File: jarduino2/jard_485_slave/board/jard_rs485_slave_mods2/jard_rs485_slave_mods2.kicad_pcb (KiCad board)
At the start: 2 copper layers, 79.2 x 30 mm, 46 parts, among them J1 POWER, J3 Débit, J4 Niveaux, J6 EV1, Q4 BPC_FMMT38C, Q6 P03P4L-04, U1 MAX485E, U6 BPC_DHT22

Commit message: Finitions avant production
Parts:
- added TP6: TestPoint, TestPoint:TestPoint_Pad_D1.5mm, B.Cu at (124.0, 103.9)
- added TP7: TestPoint, TestPoint:TestPoint_Pad_D1.5mm, B.Cu at (123.9, 98.8)
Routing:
- net BUS_A: track 19.9 -> 23.2 mm
- net BUS_B: track 22.2 -> 25.5 mm
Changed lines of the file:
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@@
     )
+  )
+  (footprint "TestPoint:TestPoint_Pad_D1.5mm" (layer "B.Cu")
+    (at 123.96 103.89 180)
+    (descr "SMD pad as test Point, diameter 1.5mm")
+    (tags "test point SMD pad")
+    (property "Price" "0")
+    (property "RefFabricant" "")
+    (property "RefFournisseur" "")
+    (property "Sheetfile" "ES.kicad_sch")
+    (property "Sheetname" "ES")
+    (property "ki_description" "test point")
+    (property "ki_keywords" "test point tp")
+    (attr exclude_from_pos_files)
+    (fp_text reference "TP6" (at 0 1.648) (layer "B.SilkS") hide
+        (effects (font (size 1 1) (thickness 0.15)) (justify mirror))
+    )
+    (fp_text value "TestPoint" (at 0 -1.75) (layer "B.Fab")
+        (effects (font (size 1 1) (thickness 0.15)) (justify mirror))
+    )
+    (fp_text user "${REFERENCE}" (at 0 1.65) (layer "B.Fab")
+        (effects (font (size 1 1) (thickness 0.15)) (justify mirror))
+    )
+    (fp_circle (center 0 0) (end 0 -0.95)
+      (stroke (width 0.12) (type solid)) (fill none) (layer "B.SilkS"))
+    (fp_circle (center 0 0) (end 1.25 0)
+      (stroke (width 0.05) (type solid)) (fill none) (layer "B.CrtYd"))
+    (pad "1" smd circle (at 0 0 180) (size 1.5 1.5) (layers "B.Cu" "B.Mask")
+      (net 17 "BUS_B") (pinfunction "1") (pintype "passive"))
   )
   (footprint "LED_THT:LED_D3.0mm_FlatTop" (layer "B.Cu")
@@
   )
   (footprint "TestPoint:TestPoint_Pad_D1.5mm" (layer "B.Cu")
+    (at 123.93 98.82 180)
+    (descr "SMD pad as test Point, diameter 1.5mm")
+    (tags "test point SMD pad")
+    (property "Price" "0")
+    (property "RefFabricant" "")
+    (property "RefFournisseur" "")
+    (property "Sheetfile" "ES.kicad_sch")
+    (property "Sheetname" "ES")
+    (property "ki_description" "test point")
+    (property "ki_keywords" "test point tp")
+    (attr exclude_from_pos_files)
+    (fp_text reference "TP7" (at 0 1.648) (layer "B.SilkS") hide
+        (effects (font (size 1 1) (thickness 0.15)) (justify mirror))
+    )
+    (fp_text value "TestPoint" (at 0 -1.75) (layer "B.Fab")
+        (effects (font (size 1 1) (thickness 0.15)) (justify mirror))
+    )
+    (fp_text user "${REFERENCE}" (at 0 1.65) (layer "B.Fab")
+        (effects (font (size 1 1) (thickness 0.15)) (justify mirror))
+    )
+    (fp_circle (center 0 0) (end 0 -0.95)
+      (stroke (width 0.12) (type solid)) (fill none) (layer "B.SilkS"))
+    (fp_circle (center 0 0) (end 1.25 0)
+      (stroke (width 0.05) (type solid)) (fill none) (layer "B.CrtYd"))
+    (pad "1" smd circle (at 0 0 180) (size 1.5 1.5) (layers "B.Cu" "B.Mask")
+      (net 16 "BUS_A") (pinfunction "1") (pintype "passive"))
+  )
+  (footprint "TestPoint:TestPoint_Pad_D1.5mm" (layer "B.Cu")
     (at 154.97 115.24 90)
     (descr "SMD pad as test Point, diameter 1.5mm")
@@
   (gr_rect (start 113.39 86.8) (end 192.39 116.8)
     (stroke (width 0.1) (type solid)) (fill none) (layer "User.1"))
+  (gr_text "A" (at 123.38 97.4 270) (layer "B.SilkS")
+    (effects (font (size 0.8 0.8) (thickness 0.1)) (justify left bottom mirror))
+  )
   (gr_text "TX" (at 145.288 92.202 90) (layer "B.SilkS")
     (effects (font (size 0.8 0.8) (thickness 0.1)) (justify left bottom mirror))
@@
     (effects (font (size 0.8 0.8) (thickness 0.1)) (justify left bottom mirror))
   )
+  (gr_text "Esclave OYA\nRev G0\nBPC 2024" (at 116.41 105.8 -90) (layer "B.SilkS")
+    (effects (font (size 1 1) (thickness 0.15)) (justify left bottom mirror))
+  )
   (gr_text "TEN" (at 145.25 97.18 90) (layer "B.SilkS")
     (effects (font (size 0.8 0.8) (thickness 0.1)) (justify left bottom mirror))
   )
+  (gr_text "B" (at 123.46 106.14 270) (layer "B.SilkS")
+    (effects (font (size 0.8 0.8) (thickness 0.1)) (justify left bottom mirror))
+  )
   (gr_text "+12V" (at 117.96 95.68 -90) (layer "B.SilkS")
     (effects (font (size 0.8 0.8) (thickness 0.1)) (justify left bottom mirror))
@@
     (effects (font (size 1 1) (thickness 0.15)) (justify left bottom))
   )
-  (gr_text "05/05/2024" (at 114.32 107.73 270) (layer "F.SilkS")
+  (gr_text "05/05/2024" (at 114.55 107.41 270) (layer "F.SilkS")
     (effects (font (size 0.8 0.8) (thickness 0.1)) (justify left bottom))
   )
@@
     (effects (font (size 0.8 0.8) (thickness 0.15)) (justify left bottom))
   )
-  (gr_text "Esclave OYA\nRev G0\nBPC 2024" (at 114.12 89.4 270) (layer "F.SilkS")
+  (gr_text "Esclave OYA\nRev G0\nBPC 2024" (at 114.77 89.8 270) (layer "F.SilkS")
     (effects (font (size 1 1) (thickness 0.15)) (justify left bottom))
   )
@@
   (via (at 141.83 104.4) (size 0.8) (drill 0.4) (layers "F.Cu" "B.Cu") (free) (net 2))
   (via (at 188.74 106.29) (size 0.8) (drill 0.4) (layers "F.Cu" "B.Cu") (net 2))
-  (via (at 114.9 98.04) (size 0.8) (drill 0.4) (layers "F.Cu" "B.Cu") (free) (net 2))
+  (via (at 114.87 98.48) (size 0.8) (drill 0.4) (layers "F.Cu" "B.Cu") (free) (net 2))
   (via (at 180.18 96.16) (size 0.8) (drill 0.4) (layers "F.Cu" "B.Cu") (free) (net 2))
   (via (at 128.93 101.47) (size 0.8) (drill 0.4) (layers "F.Cu" "B.Cu") (net 2))
@@
   (segment (start 132.57 99.46) (end 132.57 100.52) (width 0.25) (layer "B.Cu") (net 16))
   (segment (start 134.53 100.52) (end 134.67 100.38) (width 0.25) (layer "B.Cu") (net 16))
+  (segment (start 123.93 98.82) (end 127.27 98.82) (width 0.25) (layer "B.Cu") (net 16))
   (segment (start 131.93 98.82) (end 132.57 99.46) (width 0.25) (layer "B.Cu") (net 16))
   (segment (start 127.27 98.82) (end 131.93 98.82) (width 0.25) (layer "B.Cu") (net 16))
@@
   (segment (start 133.66 101.86) (end 131.62 103.9) (width 0.25) (layer "F.Cu") (net 17))
   (segment (start 127.27 103.9) (end 131.88 103.9) (width 0.25) (layer "B.Cu") (net 17))
+  (segment (start 123.97 103.9) (end 123.96 103.89) (width 0.25) (layer "B.Cu") (net 17))
   (segment (start 134.61 102.42) (end 134.67 102.48) (width 0.25) (layer "B.Cu") (net 17))
   (segment (start 132.58 103.2) (end 132.57 103.19) (width 0.25) (layer "B.Cu") (net 17))
   (segment (start 132.57 103.19) (end 132.57 102.42) (width 0.25) (layer "B.Cu") (net 17))
   (segment (start 132.57 102.42) (end 134.61 102.42) (width 0.25) (layer "B.Cu") (net 17))
+  (segment (start 127.27 103.9) (end 123.97 103.9) (width 0.25) (layer "B.Cu") (net 17))
   (segment (start 131.88 103.9) (end 132.58 103.2) (width 0.25) (layer "B.Cu") (net 17))
   (segment (start 170.54 107.532) (end 170.45 107.442) (width 0.25) (layer "B.Cu") (net 18))

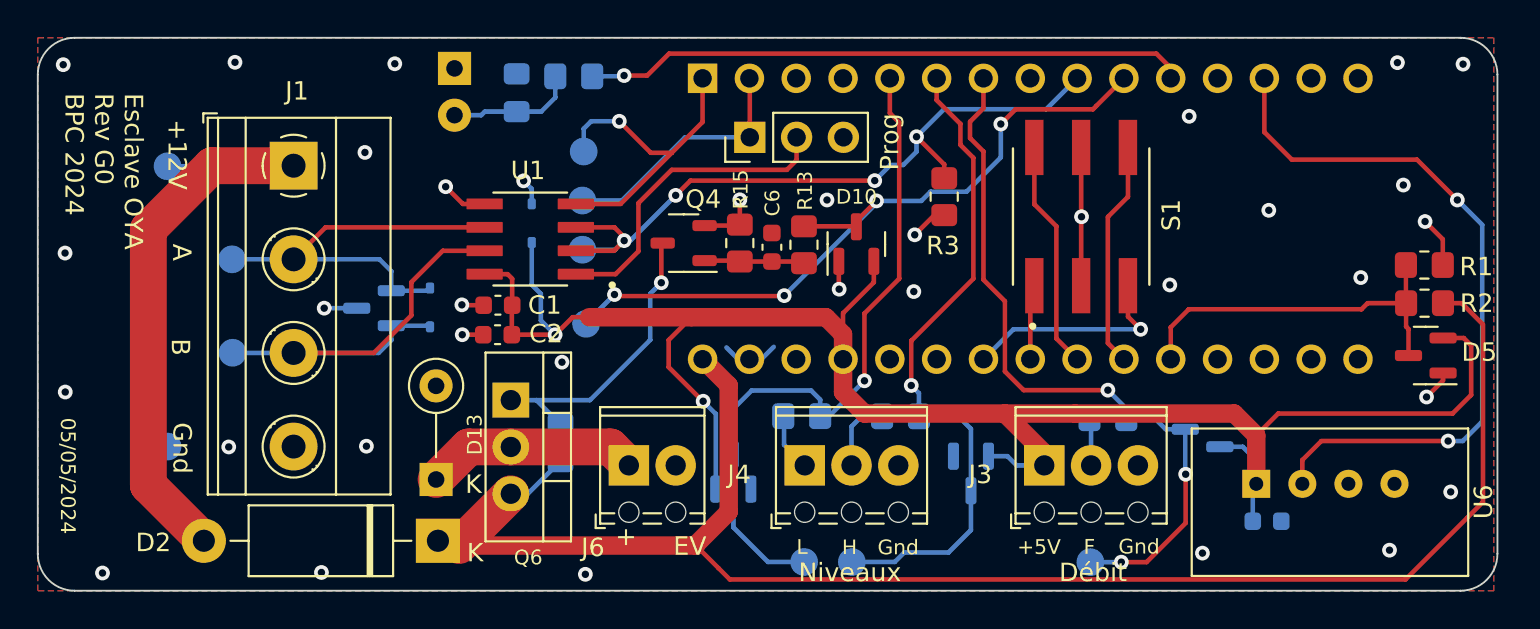
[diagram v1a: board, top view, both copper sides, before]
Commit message: Amélioration découplage RS485, MOS sur autre face
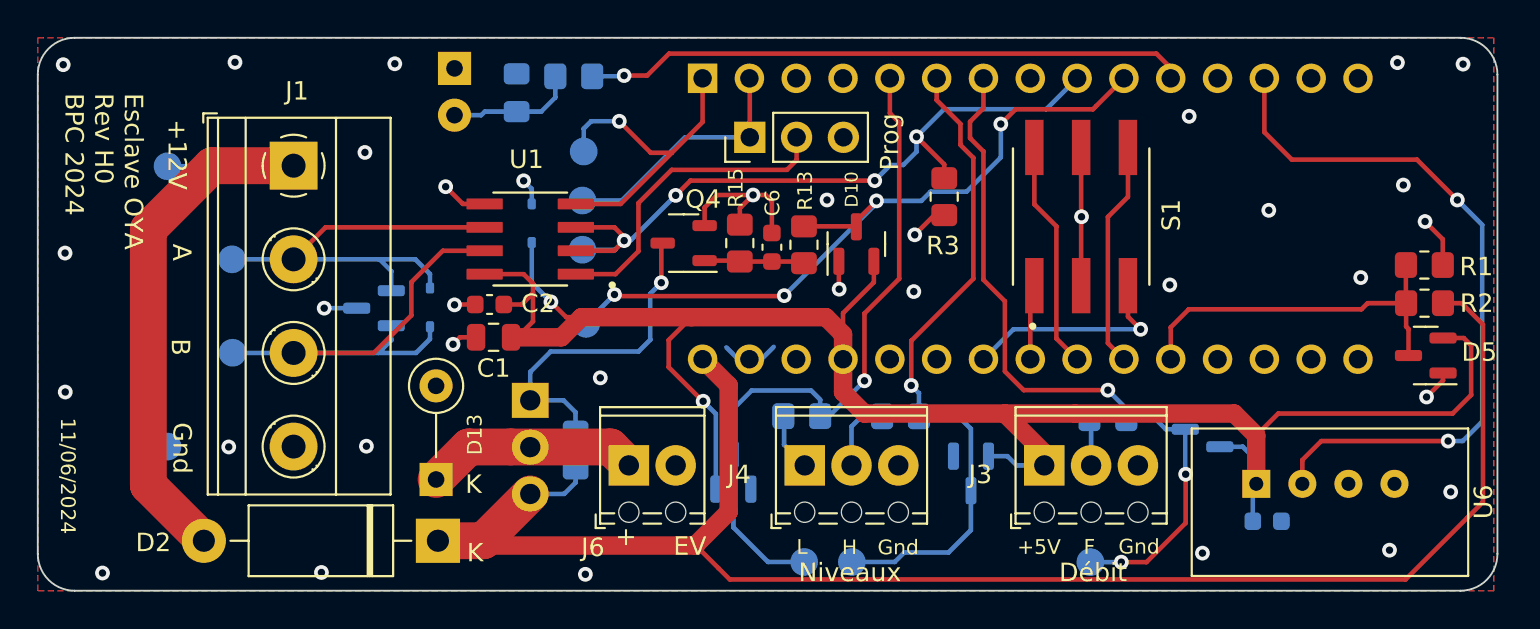
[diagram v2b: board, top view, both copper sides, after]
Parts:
- C1: value 100nF -> 10µF; footprint Capacitor_SMD:C_0603_1608Metric -> Capacitor_SMD:C_0805_2012Metric
- C2, C7: value 1nF -> 100nF
- Q6: moved to B.Cu
- moved C1 1.76 mm to (138.1, 103.0), turned to 180 degrees
- moved C2 1.70 mm to (137.9, 101.3)
- moved Q6 1.06 mm to (140.1, 106.5)
- moved R17 0.91 mm to (142.6, 109.2)
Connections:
- C1 pad 1: GND -> +5V
- C1 pad 2: +5V -> GND
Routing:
- net GND: track 29.9 -> 35.6 mm
- net +5V: track 103.2 -> 107.0 mm
- net POWER_12V: track 89.2 -> 91.3 mm
- net Net-(Q4-C): track 16.3 -> 18.1 mm
- net BUS_A: track 23.2 -> 24.9 mm
- net BUS_B: track 25.5 -> 27.2 mm
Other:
- board text added: "11/06/2024"
- board text added: "Esclave OYA Rev H0 BPC 2024"
- board text removed: "05/05/2024"
- board text removed: "Esclave OYA Rev G0 BPC 2024"
